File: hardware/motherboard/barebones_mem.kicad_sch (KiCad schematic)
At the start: 23 parts, among them Q4 MMBT3904, U30 W25Q256JWEIQ, U31 PCF85063ATL/1,118, U71 DRV5032DUDBZR, U72 PCA9306DCTR, Y5 ABS07-32.768KHZ-T

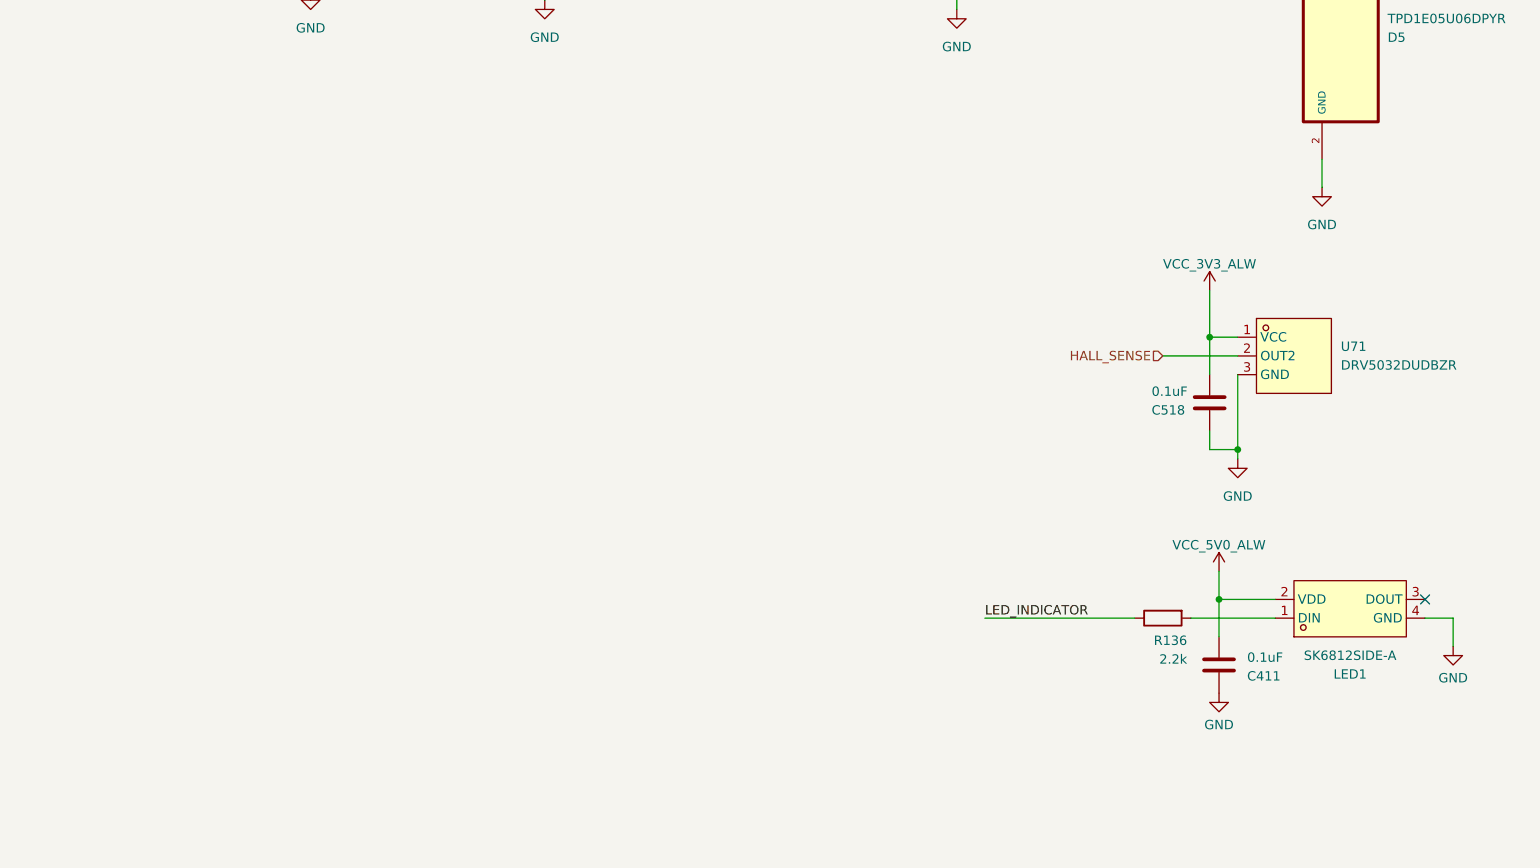
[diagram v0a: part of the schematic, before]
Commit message: pushed many changes and added dedicated bms module
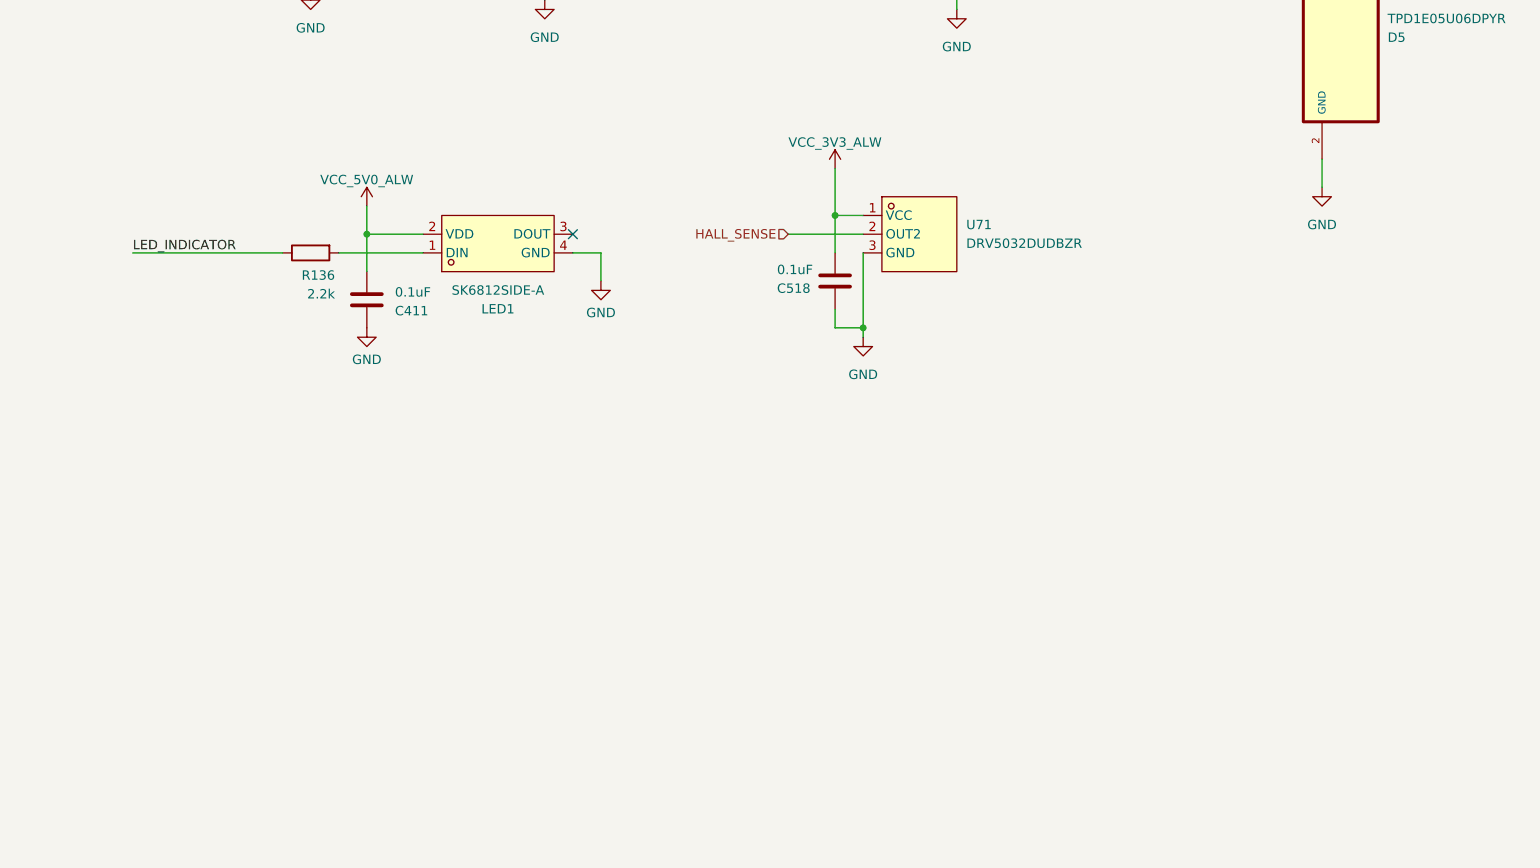
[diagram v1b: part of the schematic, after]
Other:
- moved on the sheet: C411, C518, LED1, R136, U71

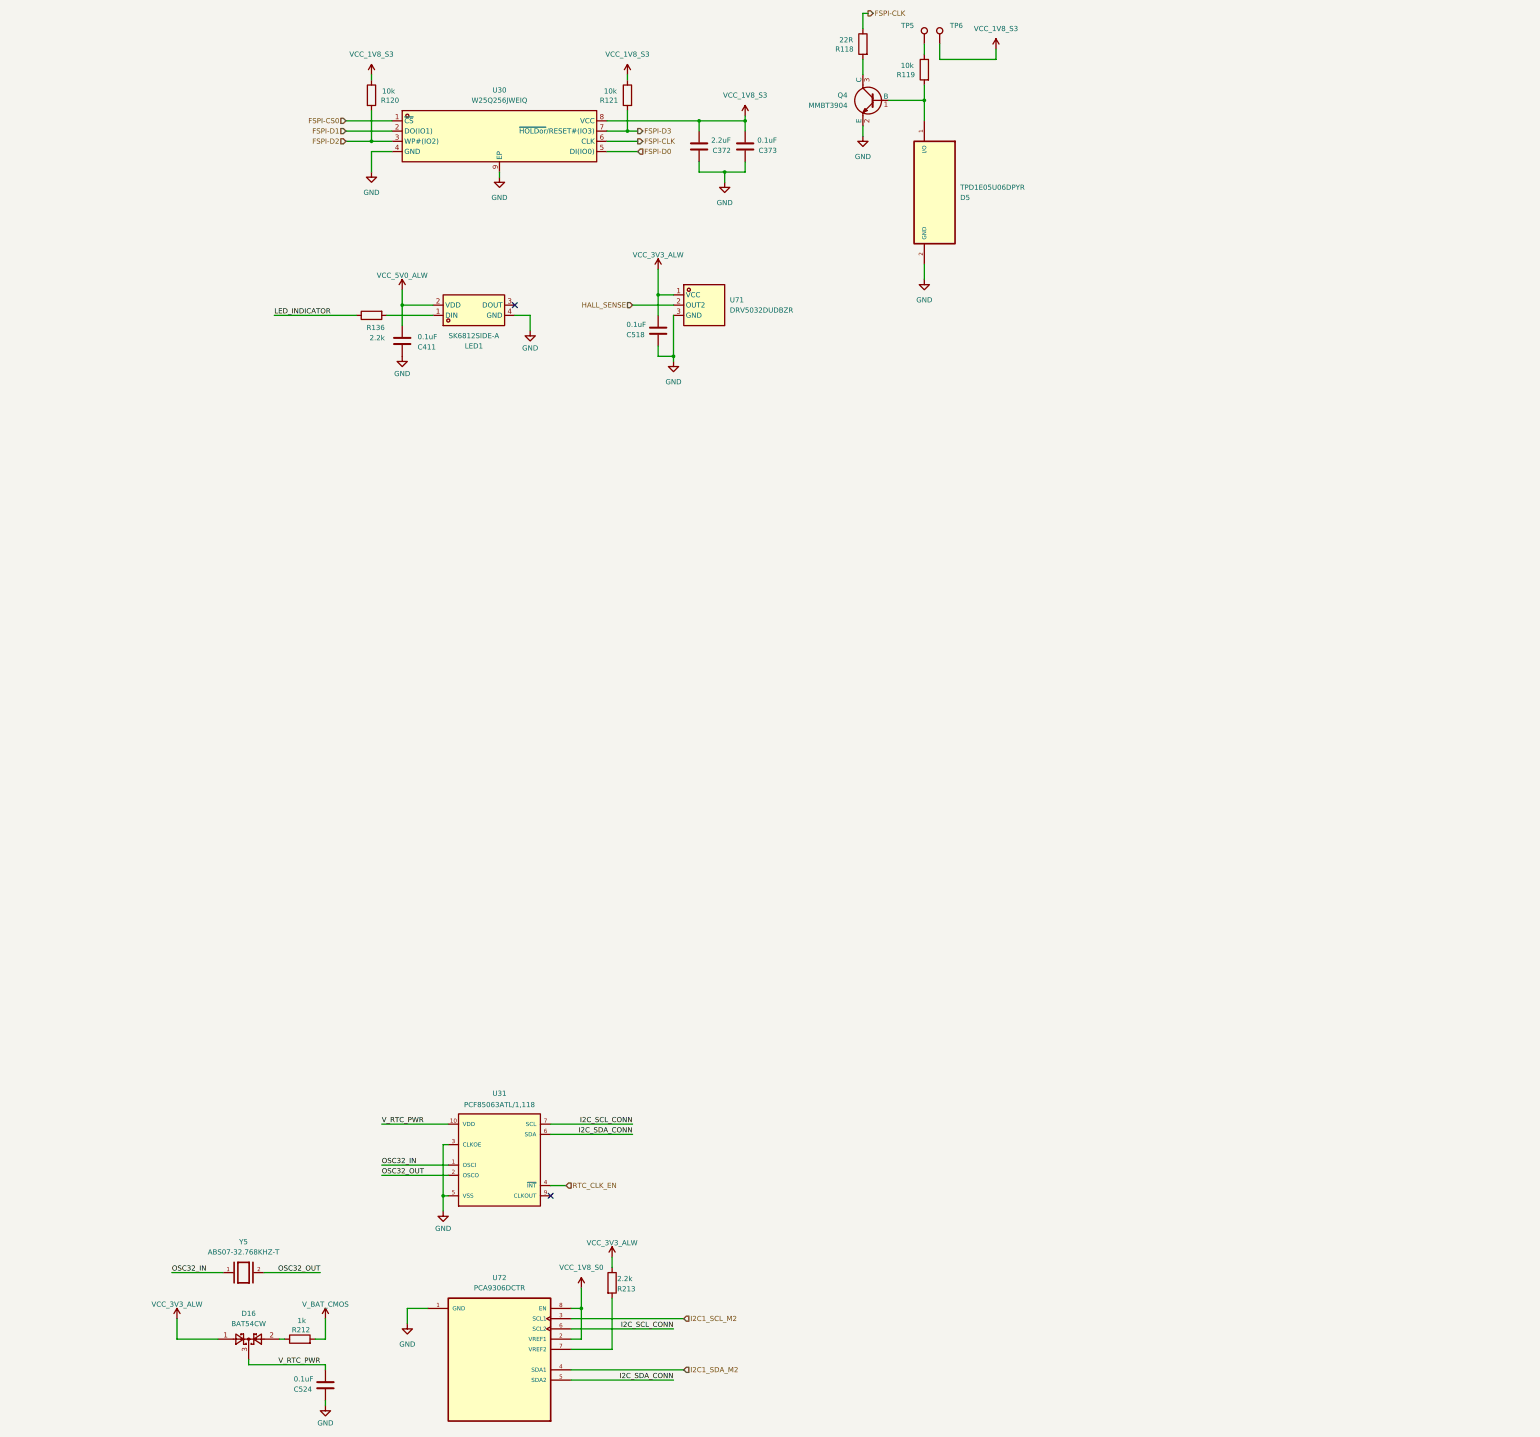
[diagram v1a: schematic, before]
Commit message: arranged the schematics in every sheet
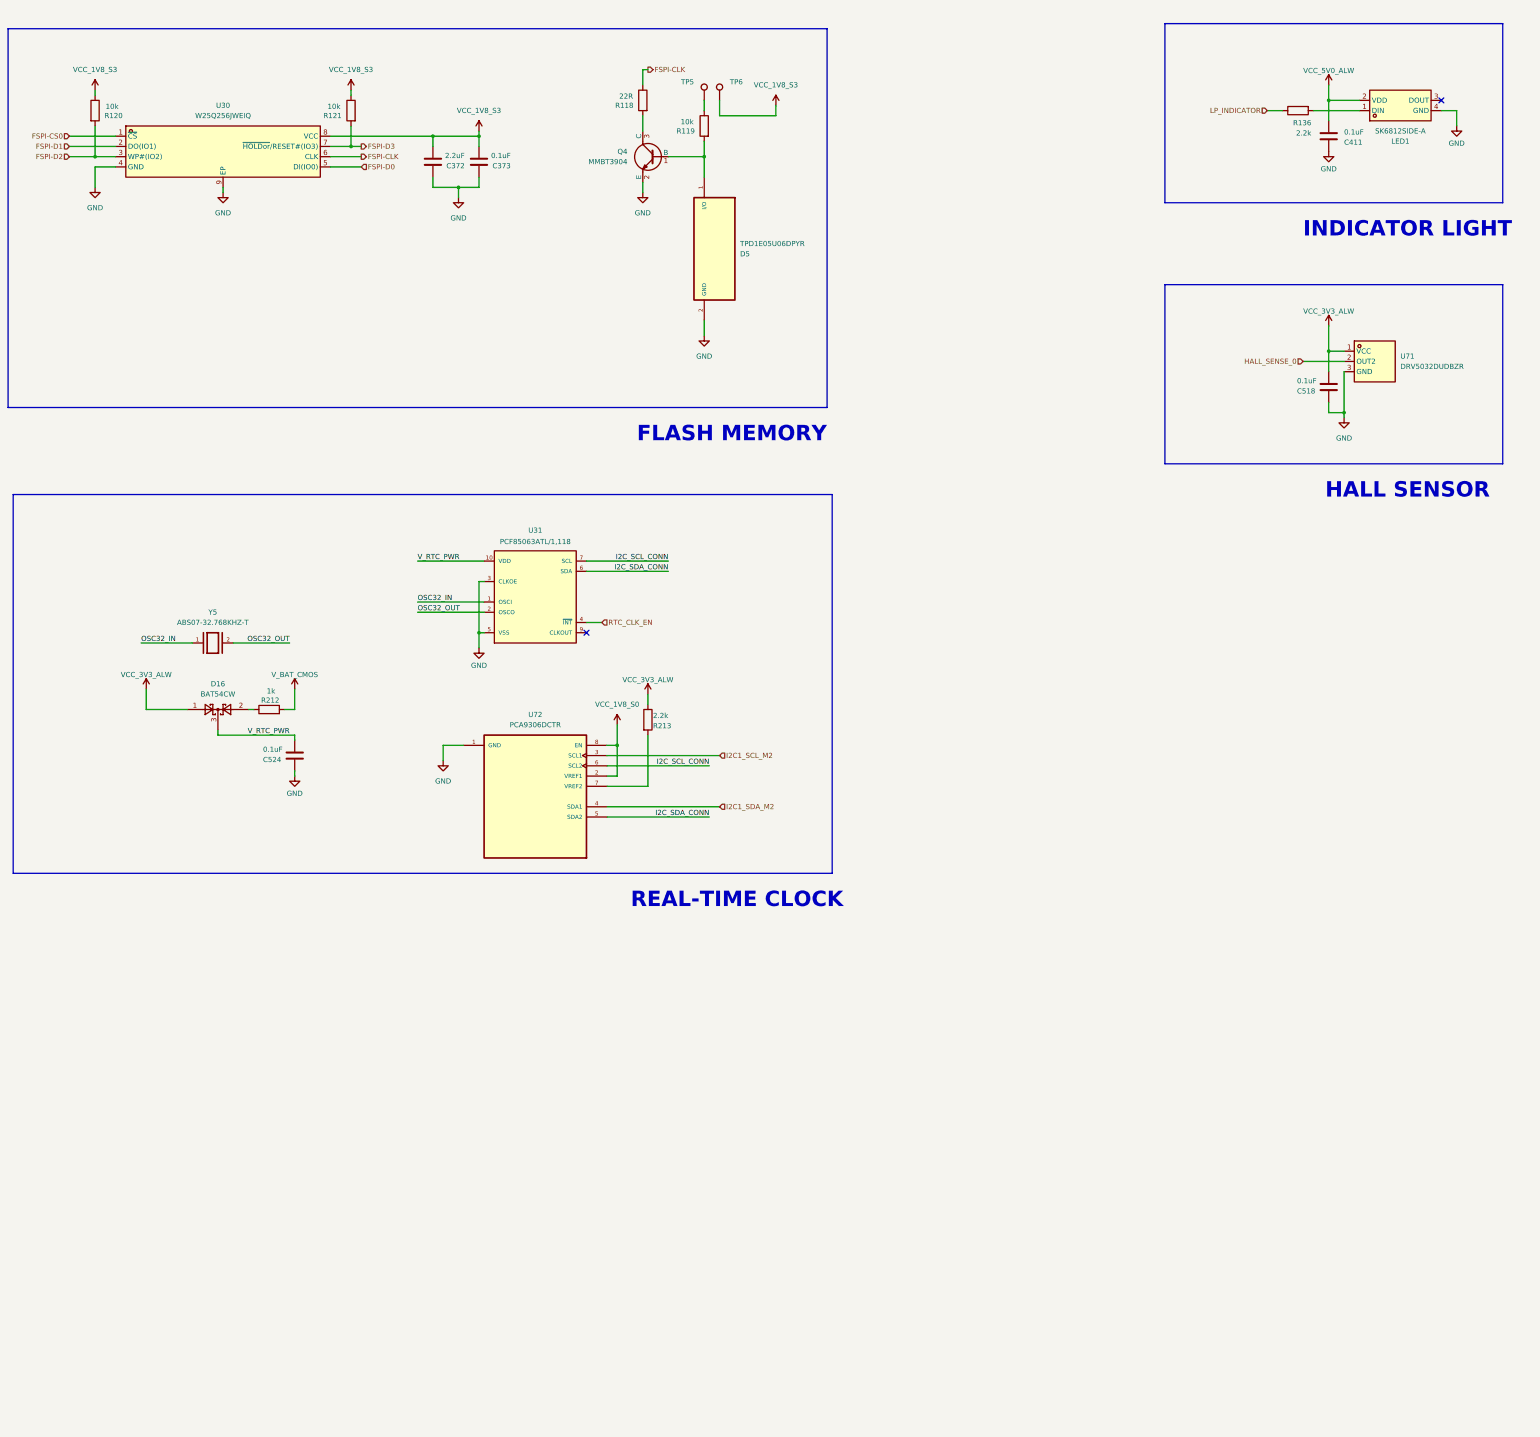
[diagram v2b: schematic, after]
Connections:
- net HALL_SENSE renamed HALL_SENSE_0
- net LED_INDICATOR renamed LP_INDICATOR
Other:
- note added: "FLASH MEMORY"
- note added: "HALL SENSOR"
- note added: "INDICATOR LIGHT"
- note added: "REAL-TIME CLOCK"
- moved on the sheet: C372, C373, C411, C518, C524, D16, D5, LED1, Q4, R118, R119, R120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

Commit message: updated last changes
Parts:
- removed R213: 2.2k, Resistor_SMD:R_0402_1005Metric, symbol Device:R
- removed U72: PCA9306DCTR, barebones:SOP65P400X130-8N, symbol PCA9306DCTR:PCA9306DCTR
- added C395, C414: 12.5pF, Capacitor_SMD:C_0603_1608Metric, symbol Device:C
- added S7: 1571983-4, barebones:SW_1571983-4, symbol 1571983-4:1571983-4
- added S8: 1-1571983-0, barebones:SW_1-1571983-0, symbol 1-1571983-0:1-1571983-0
- D5: footprint TPD1E05U06DPYR:DIO_TPD1E05U06DPYR -> barebones:DIO_TPD1E05U06DPYR
- LED1: footprint easyeda2kicad:LED-SMD_4P-L4.0-W1.6-L -> barebones:LED-SMD_4P-L4.0-W1.6-L
- Q4: footprint MMBT3904:P200_SOT-23 -> Package_TO_SOT_SMD:SOT-23
- R136: footprint Resistor_SMD:R_0603_1608Metric -> Resistor_SMD:R_0201_0603Metric
- U71: footprint easyeda2kicad:SOT-23-3_L2.9-W1.3-P1.90-LS2.4-BR -> barebones:SOT-23-3_L2.9-W1.3-P1.90-LS2.4-BR
- Y5: footprint ABS07-32.768KHZ-T:XTAL_ABS07-32.768KHZ-T -> barebones:XTAL_ABS07-32.768KHZ-T
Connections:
- net I2C_SCL_CONN is gone; now on net I2C1_SCL_M2: U31.7 (SCL)
- net I2C_SDA_CONN is gone; now on net I2C1_SDA_M2: U31.6 (SDA)
- net GND: now also C395.1, C414.1, S8.2, S8.3, S8.6, S8.7; no longer U31.3 (CLKOE)
- net OSC32_IN: now also C395.2
- net OSC32_OUT: now also C414.2
- net HALL_SENSE_0 renamed HLL_SENSOR
- net VCC_5V0_ALW renamed VCC_5V0_SYS
- new net AUDIO_PWR_1: S8.13
- new net AUDIO_PWR_2: S8.12
- new net PCIE30X1_B_EN: S8.11
- new net PCIE30X1_W_EN: S8.10
- new net PCIE30X4_PWREN_H_EN_1: S8.15
- new net PCIE30X4_PWREN_H_EN_2: S8.14
- new net VCC_3V3_S0: S8.1, S8.4, S8.5
- new net WEBCAM_PWR: S8.16
- no-connect marks 2 -> 5
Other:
- moved on the sheet: Y5

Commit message: started routing on LPDDR4x RAM
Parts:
- removed C414: 12.5pF, Capacitor_SMD:C_0603_1608Metric, symbol Device:C
- removed R119: 10k, Resistor_SMD:R_0603_1608Metric, symbol Device:R
- added C397: 12.5pF, Capacitor_SMD:C_0402_1005Metric, symbol Device:C
- added R122: 10k, Resistor_SMD:R_0402_1005Metric, symbol Device:R
- C372, C373, C395, C524: footprint Capacitor_SMD:C_0603_1608Metric -> Capacitor_SMD:C_0402_1005Metric
- R118, R120, R121, R212: footprint Resistor_SMD:R_0603_1608Metric -> Resistor_SMD:R_0402_1005Metric
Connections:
- net GND: now also C397.1
- net OSC32_OUT: now also C397.2
- net at D5.1 (I/O), Q4.1 (B): now also R122.2
- net at TP5.1: now also R122.1
